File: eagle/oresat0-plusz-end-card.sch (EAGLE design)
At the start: 36 parts, among them J1 Harwin M55-7101242R, J2 Harwin M55-7101242R, J3 Harwin M55-7101242R, J4 Harwin M55-7101242R, J6 J-SAMTEC-TFM-120-X1-XXX-D-RA, U1 QCN-19D+, U2 QCN-19D+, U3 QCN-19D+

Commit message: Final cleanup and polish of v1.1 OreSat0 +Z end card and mezzanine. Fixed S band 1/4 wave, lots of stiching and polish, fixed radial TCREAM on the contact pads, lots of TNAMES polish.
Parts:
- removed U$4, U$5, U$6, U$7, U$8: R107064070_CONTACT, J-Radiall-R107064070-RF:R107064070_CONTACT
- added J10, J11, J7, J8, J9: R107064070_CONTACT, J-Radiall-R107064070-RF:R107064070_CONTACT
- R4: value HOT -> 1 1W
- R5: value WARMISH -> 1 1W
- renumbered U$1 to J12, U$13 to J15, U$14 to J16, U$2 to J13, U$3 to J14
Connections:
- net GND: now also J10.P$2, J11.P$2, J7.P$2, J8.P$2, J9.P$2; no longer U$4.P$2, U$5.P$2, U$6.P$2, U$7.P$2, U$8.P$2
- net UHF: now also J7.P$1; no longer U$4.P$1
- net UHF_0: now also J11.P$1; no longer U$8.P$1
- net UHF_180: now also J9.P$1; no longer U$6.P$1
- net UHF_270: now also J8.P$1; no longer U$5.P$1
- net UHF_90: now also J10.P$1; no longer U$7.P$1
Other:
- note added: "MELTWIRE RESISTORS"
- note added: "PAC100001008FA1000"
- note added: "PEMSERT nuts for meltwires"

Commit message: Clean up BOM and part numbers. Ready for v1.1 fab.
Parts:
- renumbered U$10 to HW2, U$11 to HW3, U$12 to HW4, U$9 to HW1
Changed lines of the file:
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@@
 <part name="CM3" library="J-Molex-73300-003X-SMPM-M-edge-mount-NO-DIM" deviceset="J-MOLEX-SMPM-73300-003X" device=""/>
 <part name="CM2" library="J-Molex-73300-003X-SMPM-M-edge-mount-NO-DIM" deviceset="J-MOLEX-SMPM-73300-003X" device=""/>
-<part name="U$9" library="HW-mcmaster-94100A150-M2-threaded-insert" deviceset="MCMASTER-94100A150" device=""/>
-<part name="U$10" library="HW-mcmaster-94100A150-M2-threaded-insert" deviceset="MCMASTER-94100A150" device=""/>
-<part name="U$11" library="HW-mcmaster-94100A150-M2-threaded-insert" deviceset="MCMASTER-94100A150" device=""/>
-<part name="U$12" library="HW-mcmaster-94100A150-M2-threaded-insert" deviceset="MCMASTER-94100A150" device=""/>
+<part name="HW1" library="HW-mcmaster-94100A150-M2-threaded-insert" deviceset="MCMASTER-94100A150" device=""/>
+<part name="HW2" library="HW-mcmaster-94100A150-M2-threaded-insert" deviceset="MCMASTER-94100A150" device=""/>
+<part name="HW3" library="HW-mcmaster-94100A150-M2-threaded-insert" deviceset="MCMASTER-94100A150" device=""/>
+<part name="HW4" library="HW-mcmaster-94100A150-M2-threaded-insert" deviceset="MCMASTER-94100A150" device=""/>
 <part name="PCB1" library="oresat-cards" deviceset="ORESAT-CARD-V1.3-GENERIC-3RF" device=""/>
 <part name="CM1" library="J-Molex-73300-003X-SMPM-M-edge-mount-NO-DIM" deviceset="J-MOLEX-SMPM-73300-003X" device=""/>
@@
 <attribute name="VALUE" x="201.93" y="135.89" size="1.778" layer="96" rot="MR0"/>
 </instance>
-<instance part="U$9" gate="G$1" x="48.26" y="10.16" smashed="yes"/>
-<instance part="U$10" gate="G$1" x="55.88" y="10.16" smashed="yes"/>
-<instance part="U$11" gate="G$1" x="63.5" y="10.16" smashed="yes"/>
-<instance part="U$12" gate="G$1" x="71.12" y="10.16" smashed="yes"/>
+<instance part="HW1" gate="G$1" x="48.26" y="10.16" smashed="yes"/>
+<instance part="HW2" gate="G$1" x="55.88" y="10.16" smashed="yes"/>
+<instance part="HW3" gate="G$1" x="63.5" y="10.16" smashed="yes"/>
+<instance part="HW4" gate="G$1" x="71.12" y="10.16" smashed="yes"/>
 <instance part="PCB1" gate="G$1" x="58.42" y="22.86" smashed="yes"/>
 </instances>

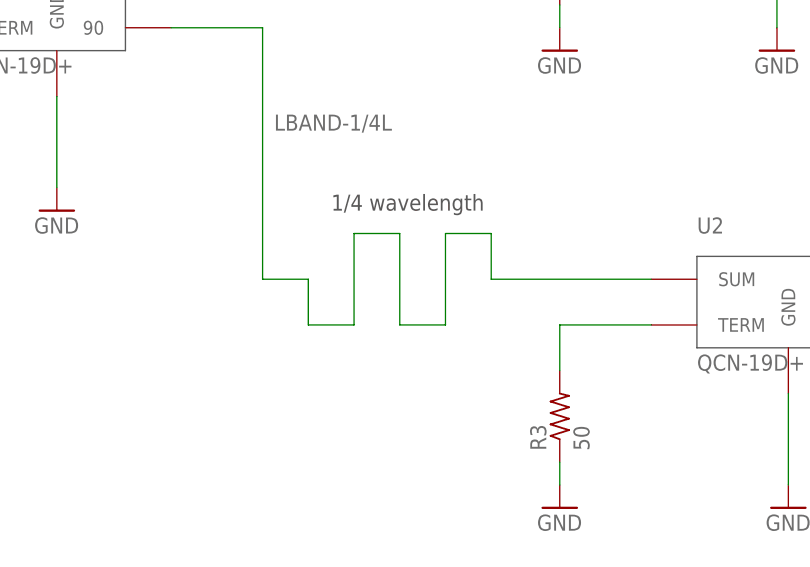
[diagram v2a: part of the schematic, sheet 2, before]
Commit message: Switched to a QCN-27D+ (with DC passthrough) for S band, and made the U and L band 1/4 wave lengths a bit more precise after getting precise lengths from Eric.
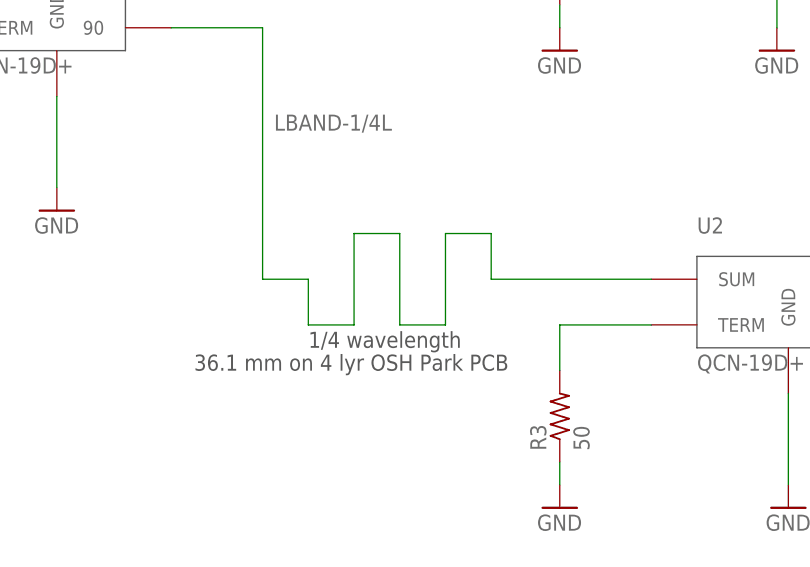
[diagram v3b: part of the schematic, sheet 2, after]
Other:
- note added: "36.1 mm on 4 lyr OSH Park PCB"
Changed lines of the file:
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@@
 <description>L BAND</description>
 <plain>
-<text x="121.92" y="104.14" size="1.778" layer="97">1/4 wavelength</text>
+<text x="119.38" y="88.9" size="1.778" layer="97">1/4 wavelength</text>
 <wire x1="218.44" y1="128.27" x2="218.44" y2="132.08" width="0.1524" layer="94"/>
 <wire x1="218.44" y1="132.08" x2="215.9" y2="135.89" width="0.1524" layer="94"/>
@@
 <text x="214.63" y="156.21" size="2.54" layer="97">4x UHF elements
 (through holes)</text>
+<text x="106.68" y="86.36" size="1.778" layer="97">36.1 mm on 4 lyr OSH Park PCB</text>
 </plain>
 <instances>

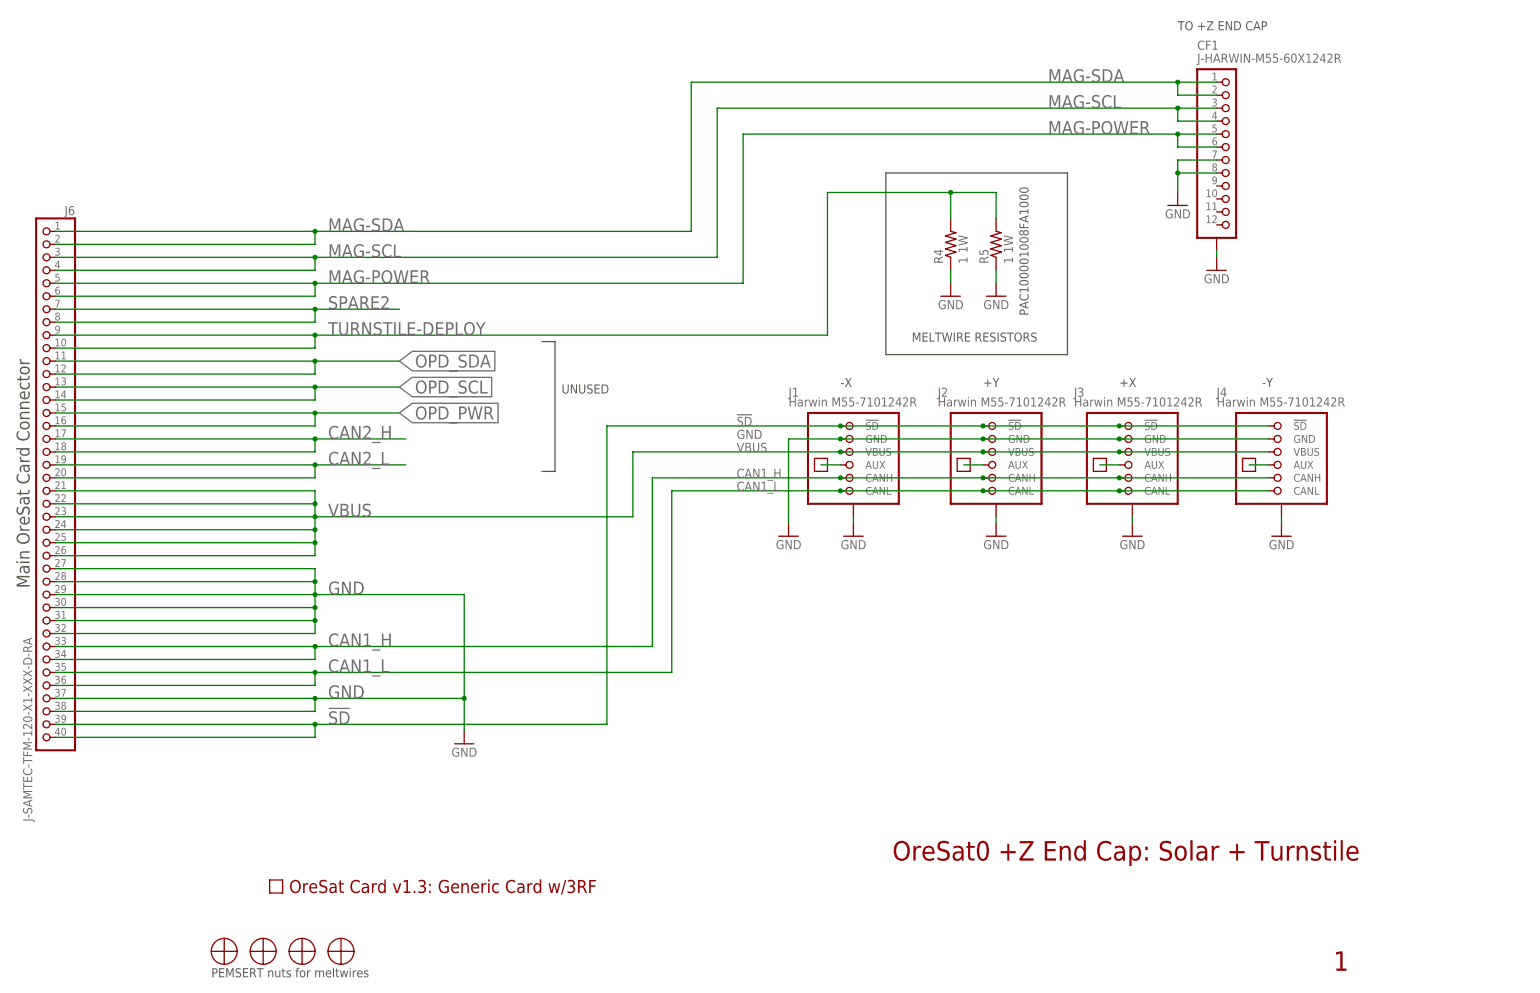
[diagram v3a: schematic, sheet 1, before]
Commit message: Small tweaks; reduced mezanine board size. Added flight tags. Off to fab!
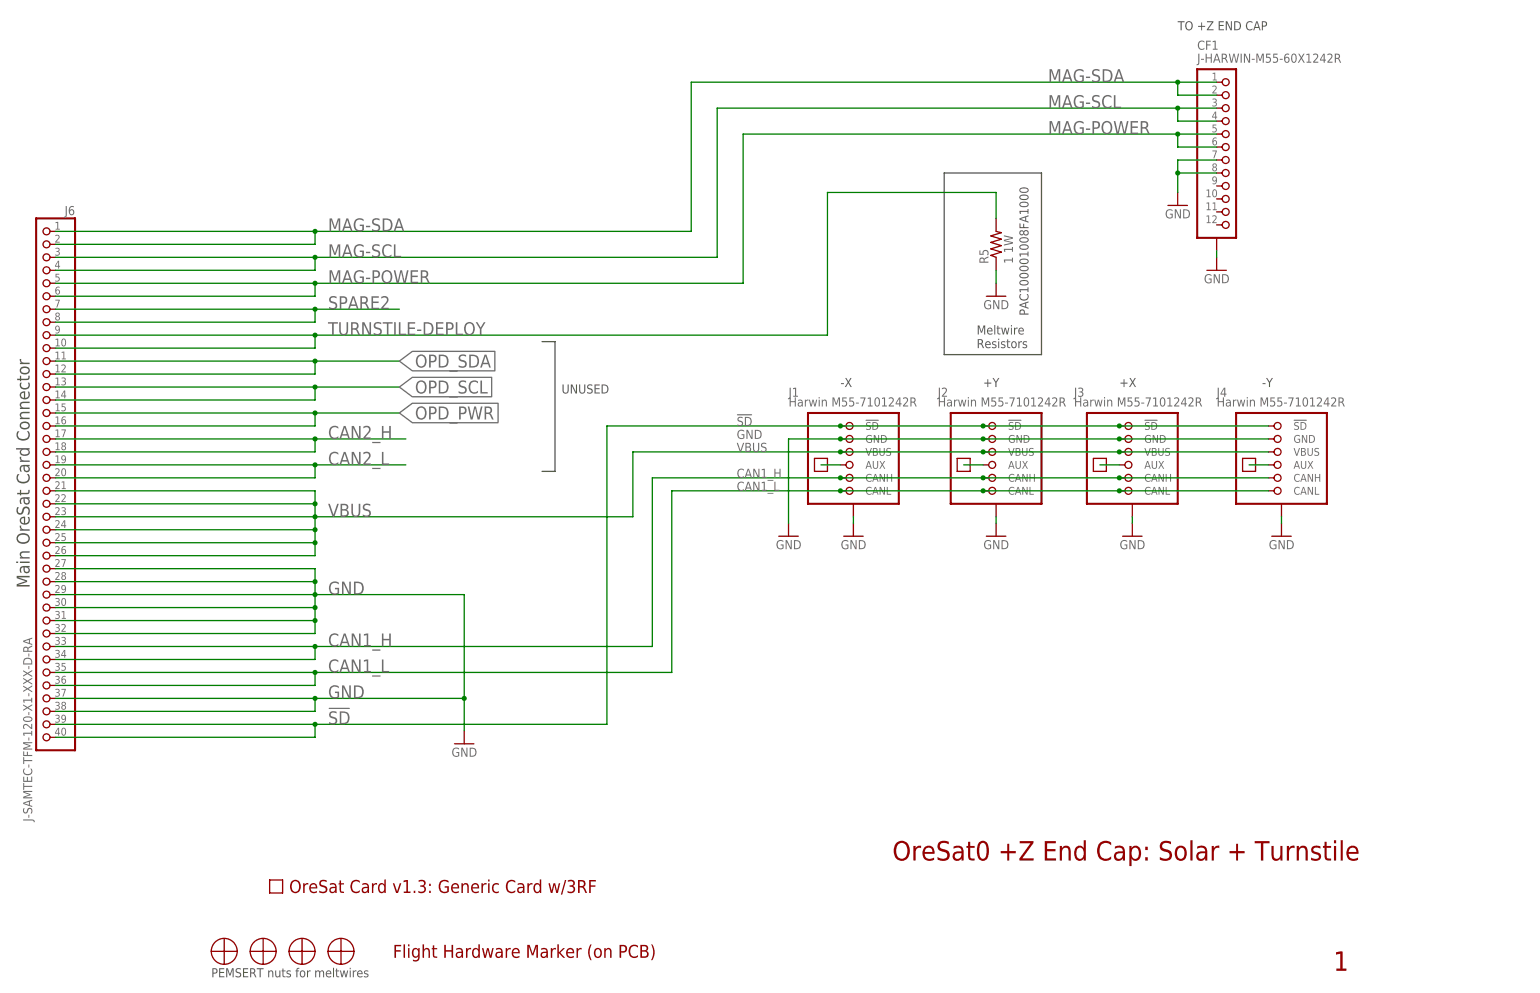
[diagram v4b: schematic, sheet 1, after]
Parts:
- removed R4: 1 1W, oresat-rcl:R-US_0309/12
- added U$1: FLIGHMARKERNEW, oresat-flight-marker:FLIGHMARKERNEW
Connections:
- net GND: no longer R4.1
- net TURNSTILE-DEPLOY: no longer R4.2
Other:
- note added: "Meltwire Resistors"
- note removed: "MELTWIRE RESISTORS"
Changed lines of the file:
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@@
 <setting verticaltext="up"/>
 </settings>
-<grid distance="0.1" unitdist="inch" unit="inch" style="lines" multiple="1" display="no" altdistance="0.01" altunitdist="inch" altunit="inch"/>
+<grid distance="0.05" unitdist="inch" unit="inch" style="lines" multiple="2" display="no" altdistance="0.01" altunitdist="inch" altunit="inch"/>
 <layers>
 <layer number="1" name="Top" color="4" fill="1" visible="no" active="no"/>
@@
 <part name="R2" library="oresat-rcl" deviceset="R-US_" device="0805-B-NOSILK" value="50"/>
 <part name="R3" library="oresat-rcl" deviceset="R-US_" device="0805-B-NOSILK" value="50"/>
-<part name="R4" library="oresat-rcl" deviceset="R-US_" device="0309/12" value="1 1W"/>
 <part name="R5" library="oresat-rcl" deviceset="R-US_" device="0309/12" value="1 1W"/>
-<part name="GND12" library="supply1" library_urn="urn:adsk.eagle:library:371" deviceset="GND" device=""/>
 <part name="GND23" library="supply1" library_urn="urn:adsk.eagle:library:371" deviceset="GND" device=""/>
 <part name="J7" library="J-Radiall-R107064070-RF" deviceset="R107064070_CONTACT" device=""/>
@@
 <part name="GND28" library="supply1" library_urn="urn:adsk.eagle:library:371" deviceset="GND" device=""/>
 <part name="GND29" library="supply1" library_urn="urn:adsk.eagle:library:371" deviceset="GND" device=""/>
+<part name="U$1" library="oresat-flight-marker" deviceset="FLIGHMARKER" device="NEW"/>
 </parts>
 <sheets>
@@
 <text x="45.72" y="5.08" size="1.778" layer="97">PEMSERT nuts for meltwires</text>
 <text x="205.74" y="134.62" size="1.778" layer="97" rot="R90">PAC100001008FA1000</text>
-<text x="182.88" y="129.54" size="1.778" layer="97">MELTWIRE RESISTORS</text>
-<wire x1="177.8" y1="127" x2="177.8" y2="162.56" width="0.1524" layer="97"/>
-<wire x1="177.8" y1="162.56" x2="213.36" y2="162.56" width="0.1524" layer="97"/>
-<wire x1="213.36" y1="162.56" x2="213.36" y2="127" width="0.1524" layer="97"/>
-<wire x1="213.36" y1="127" x2="177.8" y2="127" width="0.1524" layer="97"/>
+<text x="195.58" y="128.27" size="1.778" layer="97">Meltwire
+Resistors</text>
+<wire x1="189.23" y1="127" x2="189.23" y2="162.56" width="0.1524" layer="97"/>
+<wire x1="189.23" y1="162.56" x2="208.28" y2="162.56" width="0.1524" layer="97"/>
+<wire x1="208.28" y1="162.56" x2="208.28" y2="127" width="0.1524" layer="97"/>
+<wire x1="208.28" y1="127" x2="189.23" y2="127" width="0.1524" layer="97"/>
 </plain>
 <instances>
@@
 <attribute name="VALUE" x="237.49" y="153.67" size="1.778" layer="96" rot="MR0"/>
 </instance>
-<instance part="R4" gate="R" x="190.5" y="148.59" smashed="yes" rot="R90">
-<attribute name="NAME" x="189.0014" y="144.78" size="1.778" layer="95" rot="R90"/>
-<attribute name="VALUE" x="193.802" y="144.78" size="1.778" layer="96" rot="R90"/>
-</instance>
 <instance part="R5" gate="R" x="199.39" y="148.59" smashed="yes" rot="R90">
 <attribute name="NAME" x="197.8914" y="144.78" size="1.778" layer="95" rot="R90"/>
 <attribute name="VALUE" x="202.692" y="144.78" size="1.778" layer="96" rot="R90"/>
-</instance>
-<instance part="GND12" gate="1" x="190.5" y="138.43" smashed="yes" rot="MR0">
-<attribute name="VALUE" x="193.04" y="135.89" size="1.778" layer="96" rot="MR0"/>
 </instance>
 <instance part="GND23" gate="1" x="199.39" y="138.43" smashed="yes" rot="MR0">
@@
 <instance part="HW4" gate="G$1" x="71.12" y="10.16" smashed="yes"/>
 <instance part="PCB1" gate="G$1" x="58.42" y="22.86" smashed="yes"/>
+<instance part="U$1" gate="G$1" x="81.28" y="8.89" smashed="yes"/>
 </instances>
 <busses>
@@
 </segment>
 <segment>
-<pinref part="R4" gate="R" pin="1"/>
-<pinref part="GND12" gate="1" pin="GND"/>
-<wire x1="190.5" y1="140.97" x2="190.5" y2="143.51" width="0.1524" layer="91"/>
-</segment>
-<segment>
 <pinref part="R5" gate="R" pin="1"/>
 <pinref part="GND23" gate="1" pin="GND"/>
@@
 <wire x1="166.37" y1="130.81" x2="166.37" y2="158.75" width="0.1524" layer="91"/>
 <pinref part="R5" gate="R" pin="2"/>
-<wire x1="166.37" y1="158.75" x2="190.5" y2="158.75" width="0.1524" layer="91"/>
-<wire x1="190.5" y1="158.75" x2="199.39" y2="158.75" width="0.1524" layer="91"/>
+<wire x1="166.37" y1="158.75" x2="199.39" y2="158.75" width="0.1524" layer="91"/>
 <wire x1="199.39" y1="158.75" x2="199.39" y2="153.67" width="0.1524" layer="91"/>
-<pinref part="R4" gate="R" pin="2"/>
-<wire x1="190.5" y1="153.67" x2="190.5" y2="158.75" width="0.1524" layer="91"/>
-<junction x="190.5" y="158.75"/>
 </segment>
 </net>
